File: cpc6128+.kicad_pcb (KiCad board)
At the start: 2 copper layers, 284 x 140.5 mm, 200 parts, among them IC101 AMS40489, IC102 z80_6128, IC103 SED9420Cac, IC104 UPD765AC-2, IC105 74LS38, IC106 74LS38, IC107 74HC14, IC108 MC74HC4051N, IC109 LA6393D, IC110 41464, IC111 41464, IC112 41464, IC113 41464, IC114 AY38912, IC115 AMS40464, IC116 74HCT02, J101 rj12, J102 audio/video, J103 Jack audio, J104 POWER_JACK_6128, Q101 KTC1815Y, Q103 KTC1815Y, Q104 KTC1815Y, Q105 KTC1815Y, Q106 KTC1815Y, Q107 KTC1815Y, SW1 SW_DIP_x01, X181 40 MHz

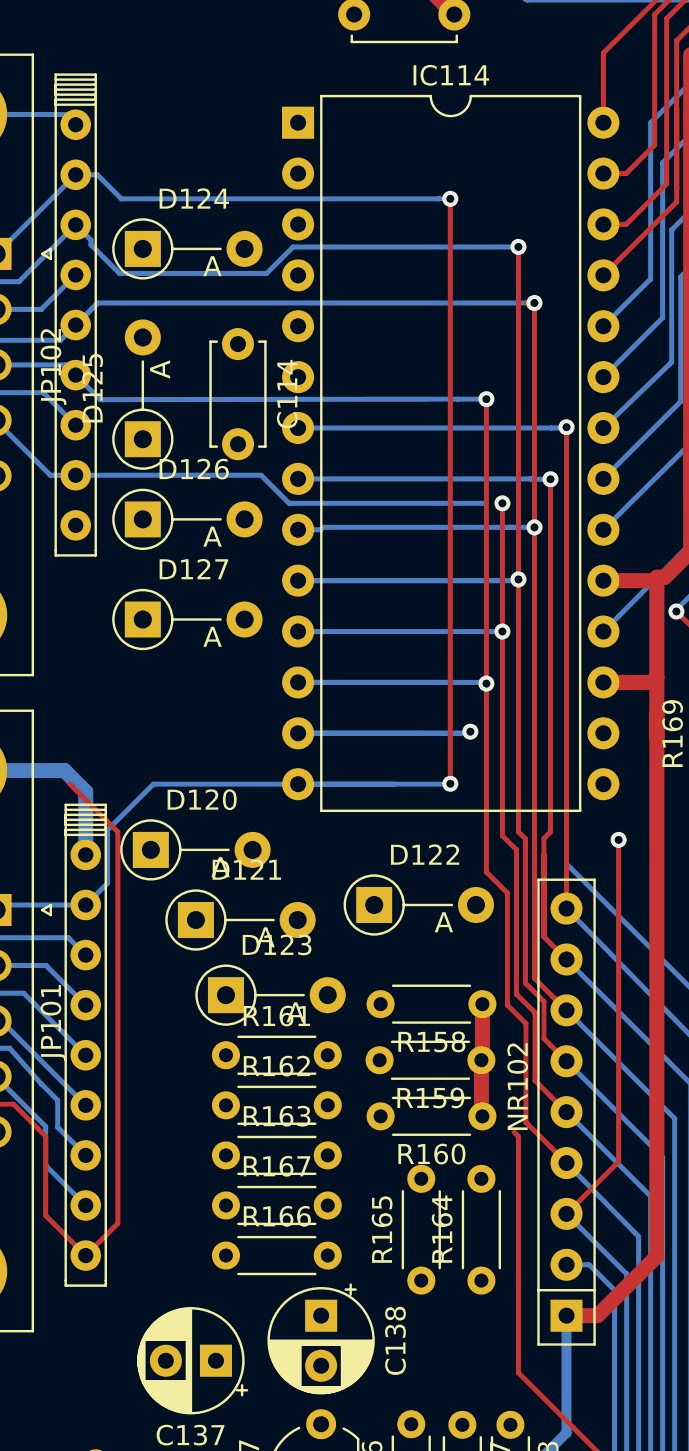
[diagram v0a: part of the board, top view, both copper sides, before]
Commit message: work on sound chip : A,B,C & X8
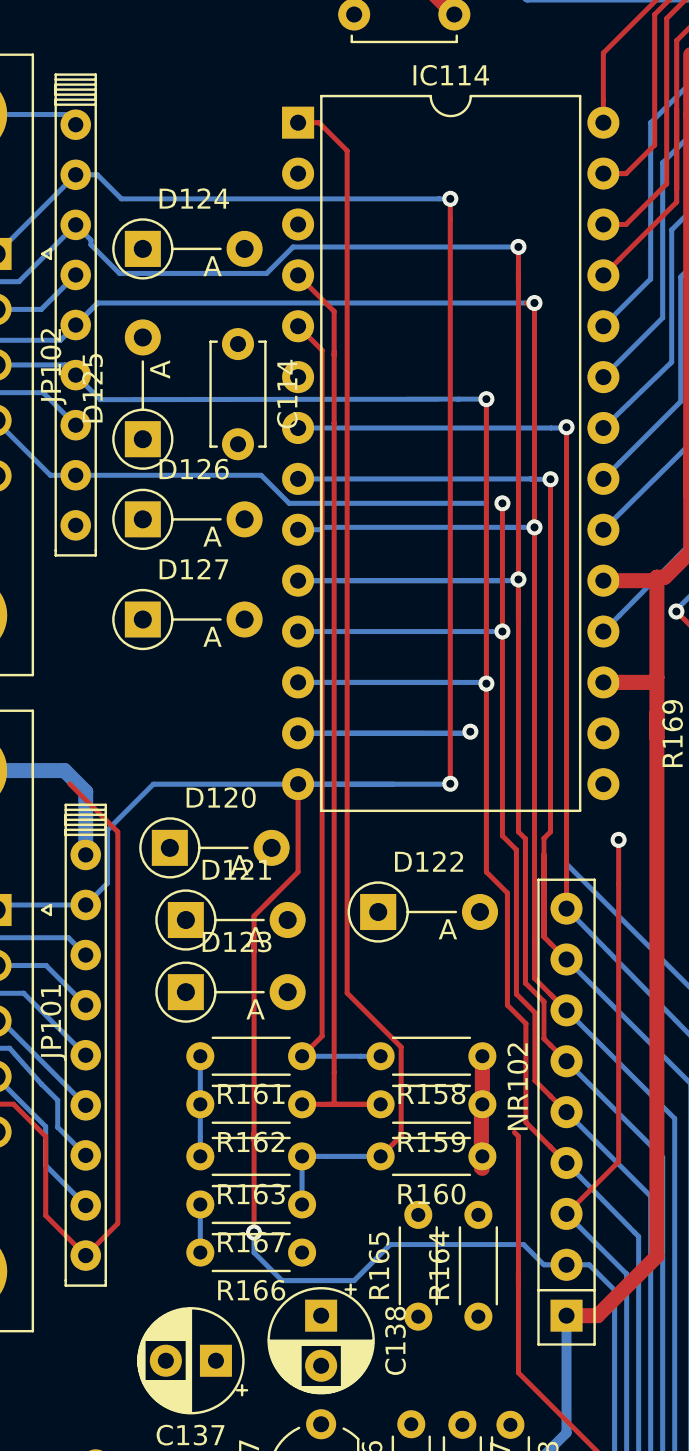
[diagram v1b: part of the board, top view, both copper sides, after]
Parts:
- moved R166 3.80 mm to (51.3, 142.6), turned to 180 degrees
- moved R161 3.80 mm to (51.3, 132.8), turned to 180 degrees
- moved R162 3.80 mm to (51.3, 135.2), turned to 180 degrees
- moved R163 3.80 mm to (51.3, 137.8), turned to 180 degrees
- moved R167 3.80 mm to (51.3, 140.2), turned to 180 degrees
- moved R158 2.60 mm to (60.3, 132.8)
- moved R159 2.20 mm to (60.3, 135.2)
- moved D123 2.01 mm to (45.5, 129.6)
- moved R160 2.00 mm to (60.3, 137.8)
- moved R164 1.81 mm to (60.1, 145.8)
- moved R165 1.81 mm to (57.1, 145.8)
- moved D120 0.96 mm to (44.7, 122.4)
- moved D121 0.50 mm to (45.5, 126.0)
- moved D122 0.40 mm to (55.1, 125.6)
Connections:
- net Net-(IC114-Pad1) renamed C
- net Net-(IC114-Pad2) renamed TST1
- net Net-(IC114-Pad4) renamed B
- net Net-(IC114-Pad5) renamed A
- C101 pad 1: +5V -> A8
- C102 pad 1: +5V -> A8
- C103 pad 1: +5V -> A8
- C104 pad 1: +5V -> A8
- C108 pad 1: +5V -> A8
- C110 pad 1: +5V -> A8
- C111 pad 1: +5V -> A8
- C112 pad 1: +5V -> A8
- C113 pad 1: +5V -> A8
- C114 pad 1: +5V -> A8
- C115 pad 1: +5V -> A8
- C117 pad 1: +5V -> A8
- C118 pad 1: +5V -> A8
- C135 pad 1: +5V -> A8
- C136 pad 1: +5V -> A8
- CP102 pad 1: +5V -> A8
- CP102 pad 2: +5V -> A8
- D110 pad 1: +5V -> A8
- IC101 pad 100: +5V -> A8
- IC101 pad 121: +5V -> A8
- IC101 pad 160: +5V -> A8
- IC101 pad 20: +5V -> A8
- IC101 pad 56: +5V -> A8
- IC102 pad 11: +5V -> A8
- IC103 pad 10: +5V -> A8
- IC103 pad 11: +5V -> A8
- IC103 pad 24: +5V -> A8
- IC104 pad 15: +5V -> A8
- IC104 pad 40: +5V -> A8
- IC107 pad 14: +5V -> (no net)
- IC107 pad 7: GND -> (no net)
- IC108 pad 1: +5V -> A8
- IC108 pad 16: +5V -> A8
- IC108 pad 2: +5V -> A8
- IC109 pad 8: +5V -> A8
- IC110 pad 9: +5V -> A8
- IC111 pad 9: +5V -> A8
- IC112 pad 9: +5V -> A8
- IC113 pad 9: +5V -> A8
- IC114 pad 17: +5V -> A8
- IC114 pad 19: +5V -> A8
- IC114 pad 3: +5V -> A8
- IC115 pad 19: +5V -> A8
- IC115 pad 20: +5V -> A8
- J101 pad 1: +5V -> A8
- JD101 pad 27: +5V -> A8
- JD102 pad 5: +5V -> A8
- JD103 pad 16: +5V -> A8
- JP102 pad 1: X8 -> Net-(JP102-Pad1)
- JP102 pad 3: X6 -> Net-(JP102-Pad3)
- JP102 pad 4: X5 -> Net-(JP102-Pad4)
- JP102 pad 6: X4 -> Net-(JP102-Pad6)
- JP102 pad 7: X3 -> Net-(JP102-Pad7)
- L104 pad 1: +5V -> A8
- NR101 pad 1: +5V -> A8
- NR102 pad 1: +5V -> A8
- Q106 pad 2: +5V -> A8
- Q107 pad 2: +5V -> A8
- R101 pad 1: +5V -> A8
- R102 pad 1: +5V -> A8
- R103 pad 1: +5V -> A8
- R107 pad 1: +5V -> A8
- R112 pad 1: +5V -> A8
- R113 pad 1: +5V -> A8
- R117 pad 1: +5V -> A8
- R118 pad 1: +5V -> A8
- R119 pad 1: +5V -> A8
- R120 pad 1: +5V -> A8
- R123 pad 1: +5V -> A8
- R124 pad 1: +5V -> A8
- R125 pad 1: +5V -> A8
- R126 pad 1: +5V -> A8
- R127 pad 1: +5V -> A8
- R193 pad 1: +5V -> A8
- R196 pad 1: +5V -> A8
- R199 pad 1: +5V -> A8
- R210 pad 1: +5V -> A8
- SW1 pad 2: +5V -> A8
- X181 pad 14: +5V -> A8
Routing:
- net +5V: track 947.2 -> 792.6 mm, vias 4 -> 3
- net A8: track 146.2 -> 300.8 mm, vias 4 -> 5
- net C: track 0.00 -> 61.1 mm
- net B: track 0.00 -> 49.0 mm
- net X8: track 177.9 -> 221.0 mm, vias 2 -> 3
- net A: track 0.00 -> 41.3 mm
- net GND: track 1262.1 -> 1267.1 mm
- net Net-(C138-Pad1): track 0.00 -> 2.40 mm

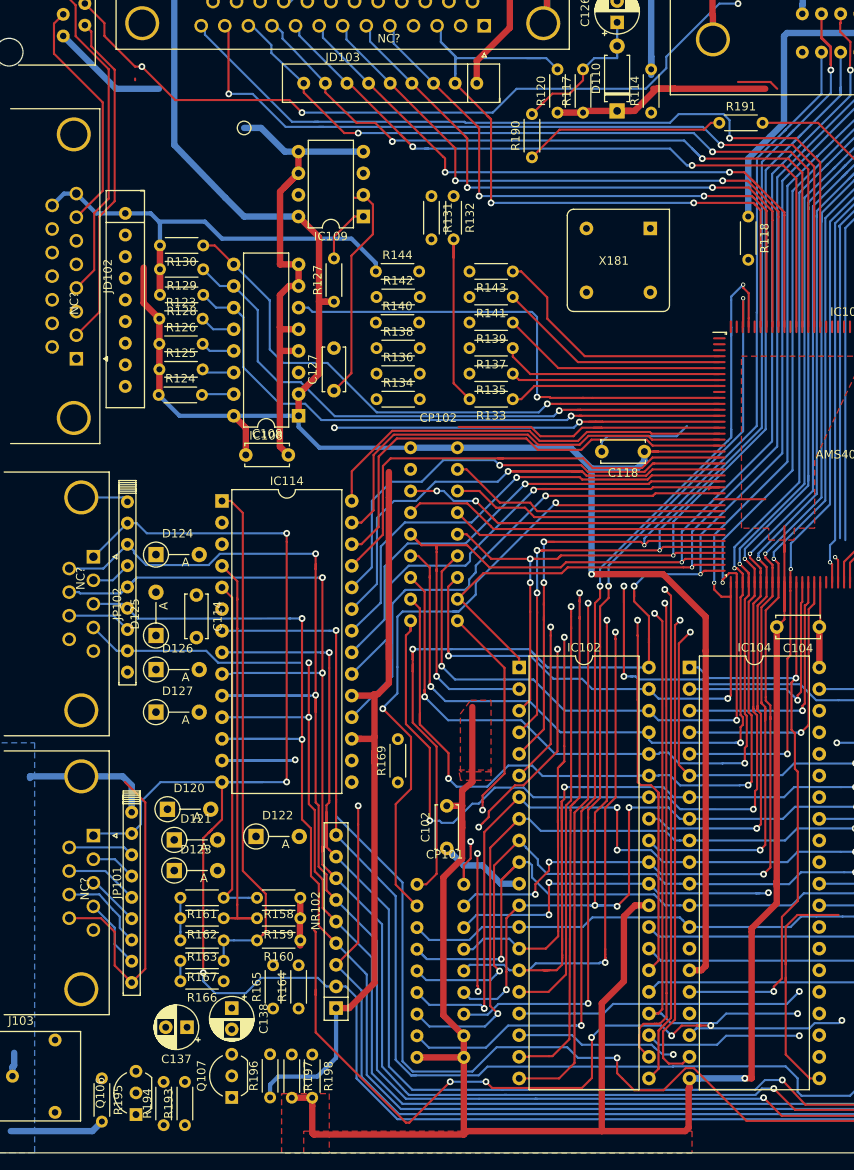
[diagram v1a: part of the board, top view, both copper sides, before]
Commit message: Work on the sound Part, close to the Audio Jack. correction of Q_NPN_ECB
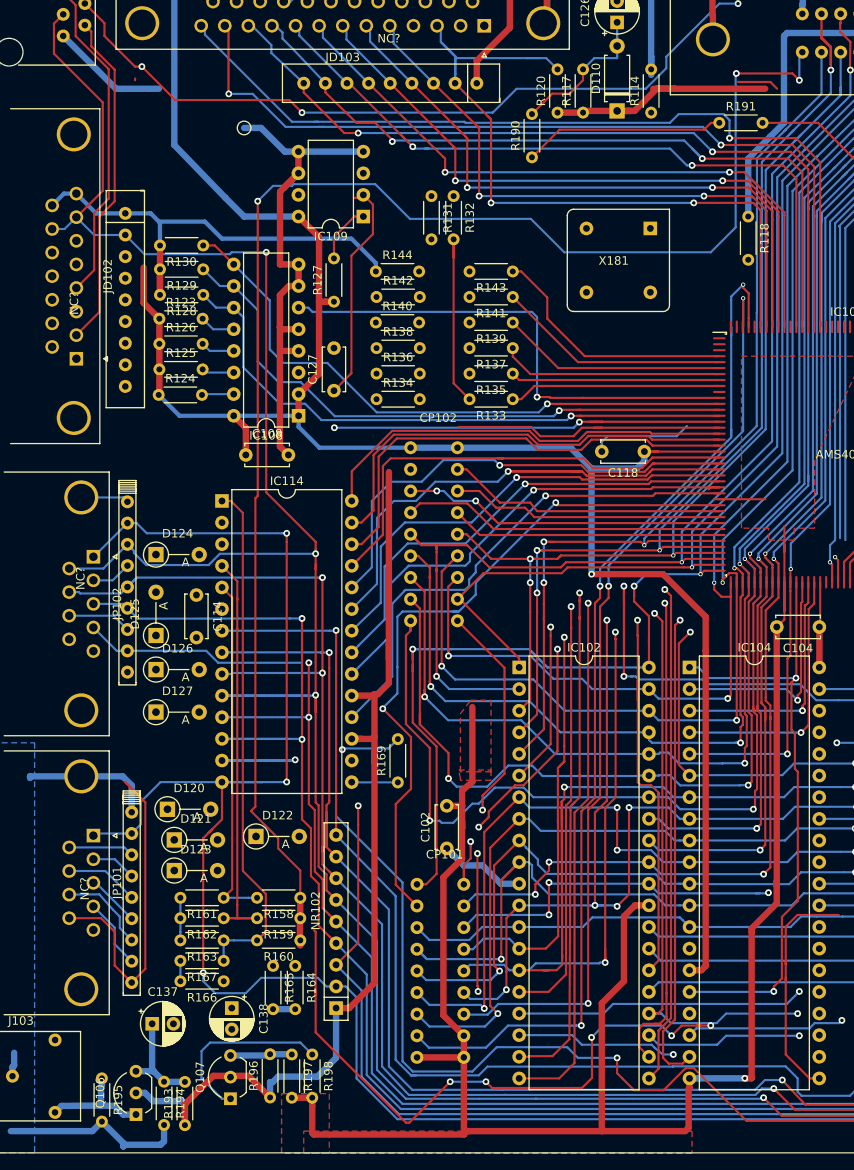
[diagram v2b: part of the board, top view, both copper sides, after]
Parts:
- moved R194 5.10 mm to (44.3, 154.4), turned to 270 degrees
- moved R164 5.02 mm to (59.7, 140.8), turned to 270 degrees
- moved R165 5.00 mm to (57.1, 140.8), turned to 270 degrees
- moved C137 4.12 mm to (42.9, 147.6), turned to 0 degrees
- moved Q107 0.21 mm to (52.1, 156.4)
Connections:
- J103 pad S: /video/L -> /video/R
- J103 pad T: /video/R -> /video/L
- NC? pad 8: (no net) -> X4
- Q106 pad 1: Net-(C137-Pad2) -> /video/L
- Q106 pad 3: /video/L -> Net-(C137-Pad1)
- Q107 pad 1: Net-(C138-Pad2) -> /video/R
- Q107 pad 3: /video/R -> Net-(C138-Pad1)
- R164 pad 2: Net-(C137-Pad1) -> Net-(C137-Pad2)
- R165 pad 2: Net-(C137-Pad1) -> Net-(C137-Pad2)
- R166 pad 2: Net-(C138-Pad1) -> Net-(C138-Pad2)
- R167 pad 2: Net-(C138-Pad1) -> Net-(C138-Pad2)
- R193 pad 2: Net-(C137-Pad2) -> Net-(C137-Pad1)
- R194 pad 1: Net-(C137-Pad2) -> Net-(C137-Pad1)
- R196 pad 2: Net-(C138-Pad2) -> Net-(C138-Pad1)
- R197 pad 1: Net-(C138-Pad2) -> Net-(C138-Pad1)
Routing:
- net SOUND: track 5.64 -> 180.9 mm, vias 0 -> 3
- net X4: track 213.6 -> 307.5 mm, vias 4 -> 5
- net /joystick/FIRE2: track 27.9 -> 0.00 mm
- net A8: track 300.8 -> 324.6 mm
- net /video/R: track 119.2 -> 140.8 mm
- net /video/L: track 8.00 -> 21.5 mm
- net CLK1: track 32.4 -> 44.9 mm, vias 0 -> 1
- net Net-(C137-Pad1): track 0.00 -> 11.9 mm
- net GND: track 1267.1 -> 1278.0 mm
- net Net-(C138-Pad1): track 2.40 -> 7.27 mm
- net Net-(C137-Pad2): track 0.00 -> 2.60 mm
- net Net-(C138-Pad2): track 0.00 -> 2.40 mm
